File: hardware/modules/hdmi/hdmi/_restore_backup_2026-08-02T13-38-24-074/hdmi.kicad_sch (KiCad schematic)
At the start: 2 parts

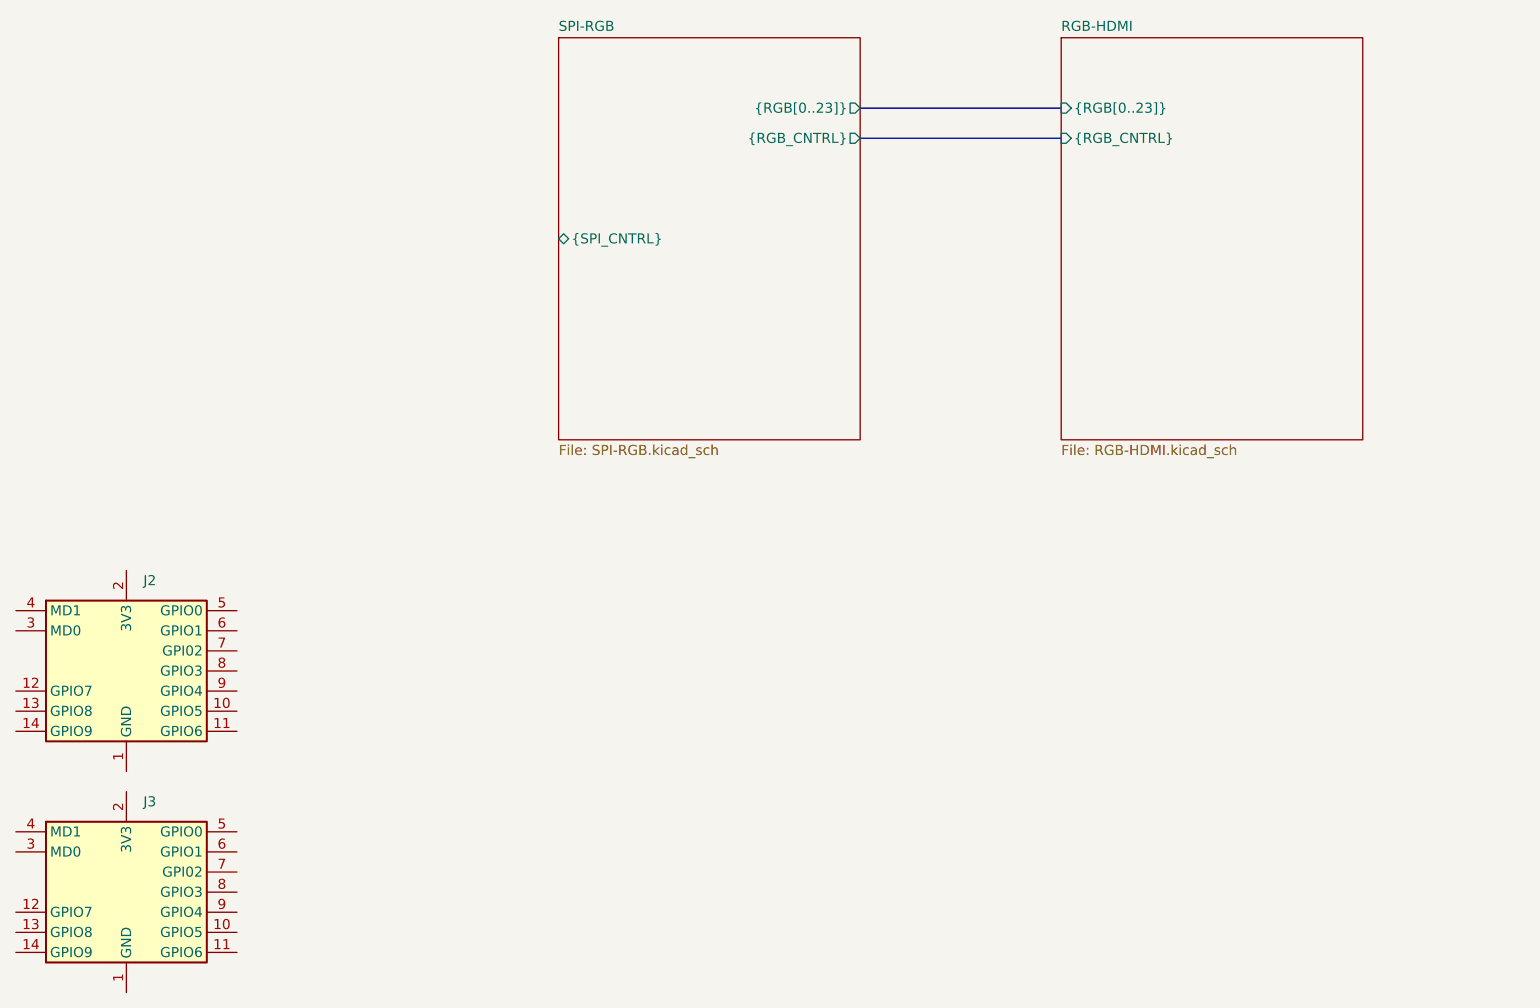
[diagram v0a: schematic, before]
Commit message: Almost finished schematic and started on layout idea's of hdmi module
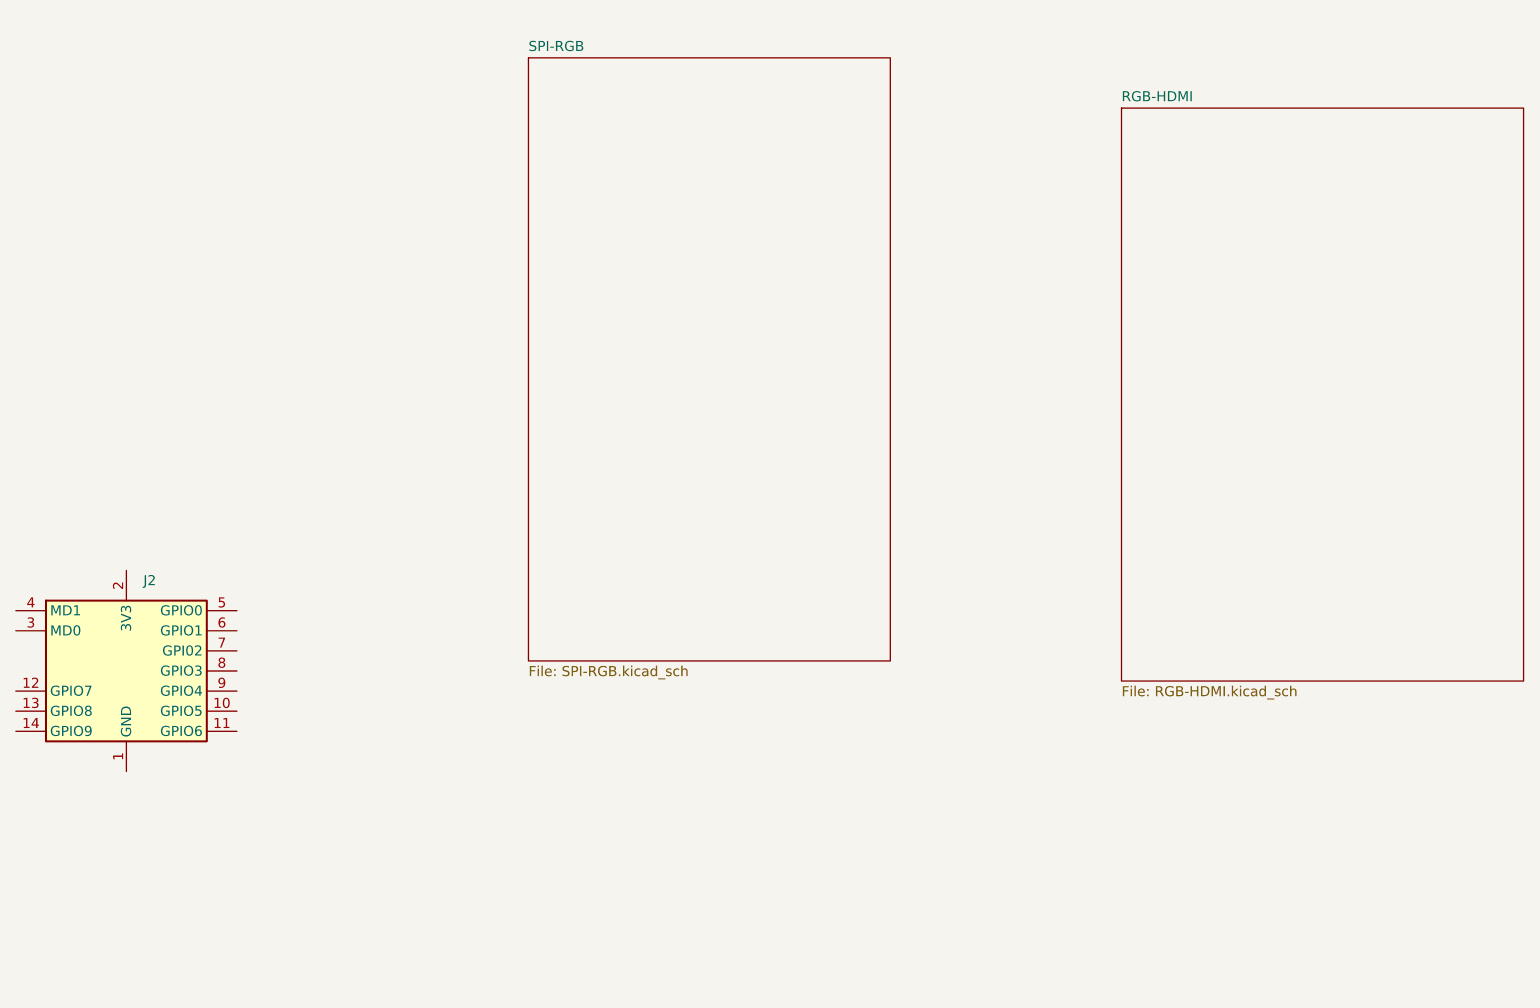
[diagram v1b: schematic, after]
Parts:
- removed J3: (no value), Connector_PinHeader_2.54mm:PinHeader_2x07_P2.54mm_Horizontal, symbol Hackxpansion:Module_Male
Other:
- sheet RGB-HDMI ports: added none; removed {RGB[0..23]}, {RGB_CNTRL}
- sheet SPI-RGB ports: added none; removed {RGB[0..23]}, {RGB_CNTRL}, {SPI_CNTRL}
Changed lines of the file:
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@@
 	(generator_version "10.0")
 	(paper "A4")
-	(bus
-		(pts
-			(xy 152.4 50.8) (xy 177.8 50.8)
-		)
-		(stroke
-			(width 0)
-			(type default)
-		)
-	)
-	(bus
-		(pts
-			(xy 152.4 46.99) (xy 177.8 46.99)
-		)
-		(stroke
-			(width 0)
-			(type default)
-		)
-	)
-	(symbol
-		(lib_id "Hackxpansion:Module_Male")
-		(at 59.69 146.05 0)
-		(unit 1)
-		(body_style 1)
-		(exclude_from_sim no)
-		(in_bom yes)
-		(on_board yes)
-		(in_pos_files yes)
-		(dnp no)
-		(fields_autoplaced yes)
-		(property "Reference" "J3"
-			(at 61.8333 134.62 0)
-			(show_name no)
-			(do_not_autoplace no)
-			(effects
-				(font
-					(size 1.27 1.27)
-				)
-				(justify left)
-			)
-		)
-		(property "Value" ""
-			(at 59.69 146.05 0)
-			(show_name no)
-			(do_not_autoplace no)
-			(effects
-				(font
-					(size 1.27 1.27)
-				)
-			)
-		)
-		(property "Footprint" "Connector_PinHeader_2.54mm:PinHeader_2x07_P2.54mm_Horizontal"
-			(at 60.96 118.11 0)
-			(hide yes)
-			(show_name no)
-			(do_not_autoplace no)
-			(effects
-				(font
-					(size 1.27 1.27)
-				)
-			)
-		)
-		(property "Datasheet" ""
-			(at 59.69 146.05 0)
-			(hide yes)
-			(show_name no)
-			(do_not_autoplace no)
-			(effects
-				(font
-					(size 1.27 1.27)
-				)
-			)
-		)
-		(property "Description" ""
-			(at 59.69 146.05 0)
-			(hide yes)
-			(show_name no)
-			(do_not_autoplace no)
-			(effects
-				(font
-					(size 1.27 1.27)
-				)
-			)
-		)
-		(pin "8"
-		)
-		(pin "14"
-		)
-		(pin "3"
-		)
-		(pin "6"
-		)
-		(pin "7"
-		)
-		(pin "13"
-		)
-		(pin "11"
-		)
-		(pin "2"
-		)
-		(pin "1"
-		)
-		(pin "12"
-		)
-		(pin "10"
-		)
-		(pin "9"
-		)
-		(pin "5"
-		)
-		(pin "4"
-		)
-		(instances
-			(project "hdmi"
-				(path "/a8055f97-0b92-4f0a-bbea-b4ab733d1ae8"
-					(reference "J3")
-					(unit 1)
-				)
-			)
-		)
-	)
 	(symbol
 		(lib_id "Hackxpansion:Module_Male")
@@
 	)
 	(sheet
-		(at 114.3 38.1)
-		(size 38.1 50.8)
+		(at 110.49 40.64)
+		(size 45.72 76.2)
 		(exclude_from_sim no)
 		(in_bom yes)
@@
 		)
 		(property "Sheetname" "SPI-RGB"
-			(at 114.3 37.3884 0)
+			(at 110.49 39.9284 0)
 			(show_name no)
 			(do_not_autoplace no)
@@
 		)
 		(property "Sheetfile" "SPI-RGB.kicad_sch"
-			(at 114.3 89.4846 0)
+			(at 110.49 117.4246 0)
 			(show_name no)
 			(do_not_autoplace no)
@@
 				)
 				(justify left top)
-			)
-		)
-		(pin "{RGB_CNTRL}" output
-			(at 152.4 50.8 0)
-			(effects
-				(font
-					(size 1.27 1.27)
-				)
-				(justify right)
-			)
-		)
-		(pin "{RGB[0..23]}" output
-			(at 152.4 46.99 0)
-			(effects
-				(font
-					(size 1.27 1.27)
-				)
-				(justify right)
-			)
-		)
-		(pin "{SPI_CNTRL}" bidirectional
-			(at 114.3 63.5 180)
-			(effects
-				(font
-					(size 1.27 1.27)
-				)
-				(justify left)
 			)
 		)
@@
 	)
 	(sheet
-		(at 177.8 38.1)
-		(size 38.1 50.8)
+		(at 185.42 46.99)
+		(size 50.8 72.39)
 		(exclude_from_sim no)
 		(in_bom yes)
@@
 		)
 		(property "Sheetname" "RGB-HDMI"
-			(at 177.8 37.3884 0)
+			(at 185.42 46.2784 0)
 			(show_name no)
 			(do_not_autoplace no)
@@
 		)
 		(property "Sheetfile" "RGB-HDMI.kicad_sch"
-			(at 177.8 89.4846 0)
+			(at 185.42 119.9646 0)
 			(show_name no)
 			(do_not_autoplace no)
@@
 			)
 		)
-		(pin "{RGB[0..23]}" input
-			(at 177.8 46.99 180)
-			(effects
-				(font
-					(size 1.27 1.27)
-				)
-				(justify left)
-			)
-		)
-		(pin "{RGB_CNTRL}" input
-			(at 177.8 50.8 180)
-			(effects
-				(font
-					(size 1.27 1.27)
-				)
-				(justify left)
-			)
-		)
